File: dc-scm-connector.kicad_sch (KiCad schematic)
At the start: 2 parts, among them J1 Socket_DC-SCM-2.1_2x84_Rev-1-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

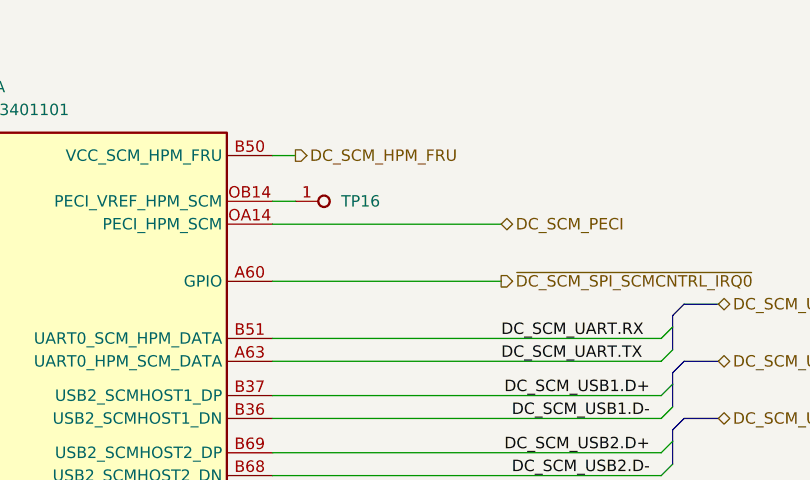
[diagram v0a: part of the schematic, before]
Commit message: [#93949] Change testpads to 1.5mm, change QSPI and UART testpad to smd technology
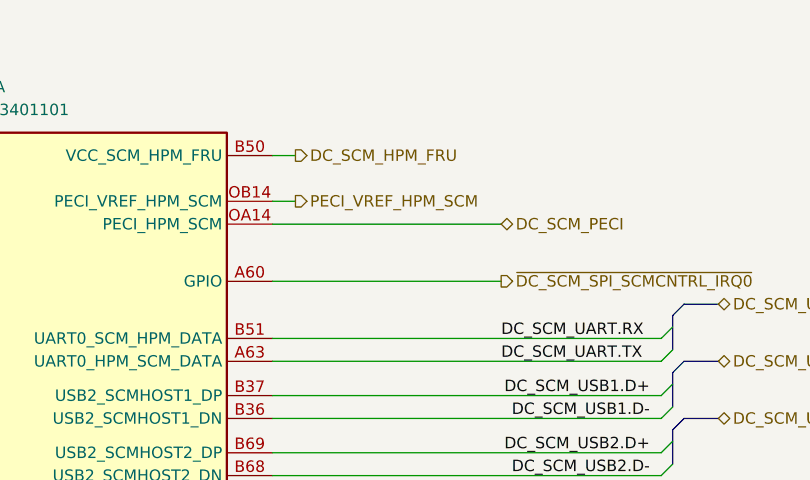
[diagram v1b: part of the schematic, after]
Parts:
- removed TP16: TP_0.75mm_SMD, antmicro-footprints:TP_SMD_0.75mm, symbol antmicroTestPoints:TP_0.75mm_SMD
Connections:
- net PECI_VREF_HPM_SCM: now reaches J1.OB14 (PECI_VREF_HPM_SCM)
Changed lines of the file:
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@@
+		)
+	)
+	(hierarchical_label "PECI_VREF_HPM_SCM"
+		(shape output)
+		(at 149.86 49.53 0)
+		(effects
+			(font
+				(size 1.27 1.27)
+			)
+			(justify left)
 		)
 	)
@@
 				)
 			)
-		)
-	)
-	(symbol
-		(lib_id "antmicroTestPoints:TP_0.75mm_SMD")
-		(at 149.86 49.53 0)
-		(unit 1)
-		(exclude_from_sim no)
-		(in_bom no)
-		(on_board yes)
-		(dnp no)
-		(property "Reference" "TP16"
-			(at 154.94 49.53 0)
-			(effects
-				(font
-					(size 1.27 1.27)
-					(thickness 0.15)
-				)
-				(justify left)
-			)
-		)
-		(property "Value" "TP_0.75mm_SMD"
-			(at 160.02 53.34 0)
-			(effects
-				(font
-					(size 1.27 1.27)
-					(thickness 0.15)
-				)
-				(justify left bottom)
-				(hide yes)
-			)
-		)
-		(property "Footprint" "antmicro-footprints:TP_SMD_0.75mm"
-			(at 160.02 55.88 0)
-			(effects
-				(font
-					(size 1.27 1.27)
-					(thickness 0.15)
-				)
-				(justify left bottom)
-				(hide yes)
-			)
-		)
-		(property "Datasheet" ""
-			(at 167.64 62.23 0)
-			(effects
-				(font
-					(size 1.27 1.27)
-					(thickness 0.15)
-				)
-				(justify left bottom)
-				(hide yes)
-			)
-		)
-		(property "Description" "SMT test point"
-			(at 160.655 63.5 0)
-			(effects
-				(font
-					(size 1.27 1.27)
-				)
-				(justify left bottom)
-				(hide yes)
-			)
-		)
-		(property "MPN" ""
-			(at 160.655 60.96 0)
-			(effects
-				(font
-					(size 1.27 1.27)
-					(thickness 0.15)
-				)
-				(justify left bottom)
-				(hide yes)
-			)
-		)
-		(property "Manufacturer" ""
-			(at 160.655 55.88 0)
-			(effects
-				(font
-					(size 1.27 1.27)
-					(thickness 0.15)
-				)
-				(justify left bottom)
-				(hide yes)
-			)
-		)
-		(property "Author" "Antmicro"
-			(at 160.02 58.42 0)
-			(effects
-				(font
-					(size 1.27 1.27)
-					(thickness 0.15)
-				)
-				(justify left bottom)
-				(hide yes)
-			)
-		)
-		(property "License" "Apache-2.0"
-			(at 160.02 60.96 0)
-			(effects
-				(font
-					(size 1.27 1.27)
-					(thickness 0.15)
-				)
-				(justify left bottom)
-				(hide yes)
-			)
-		)
-		(pin "1"
-		)
-		(instances
-			(project "bmc-breakout-board"
-				(path "/5d67ef28-5805-4f87-b722-2926dabf7f6e/bae8cef5-57a9-4ec0-acbe-6dac48c5cdf5"
-					(reference "TP16")
-					(unit 1)
-				)
-			)

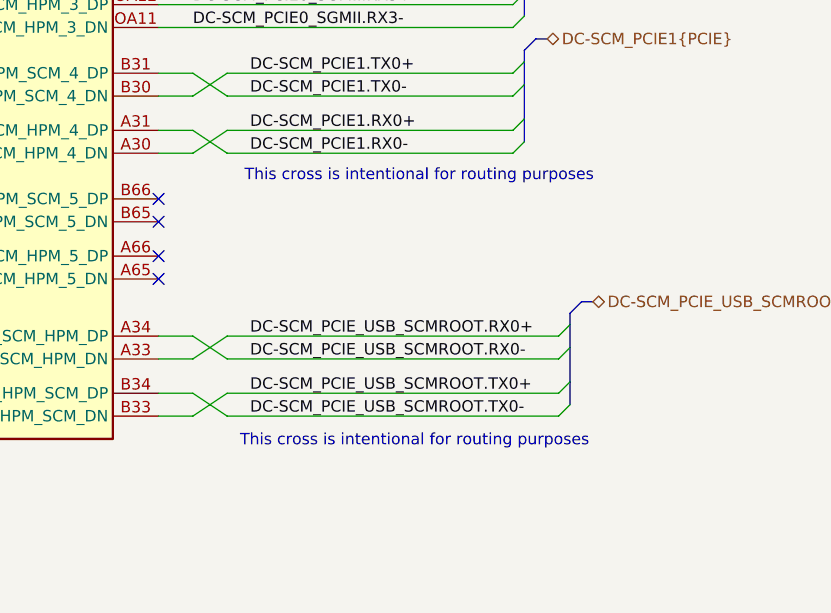
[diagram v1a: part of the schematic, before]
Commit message: [#93949] Align items to grid, change TP for UART
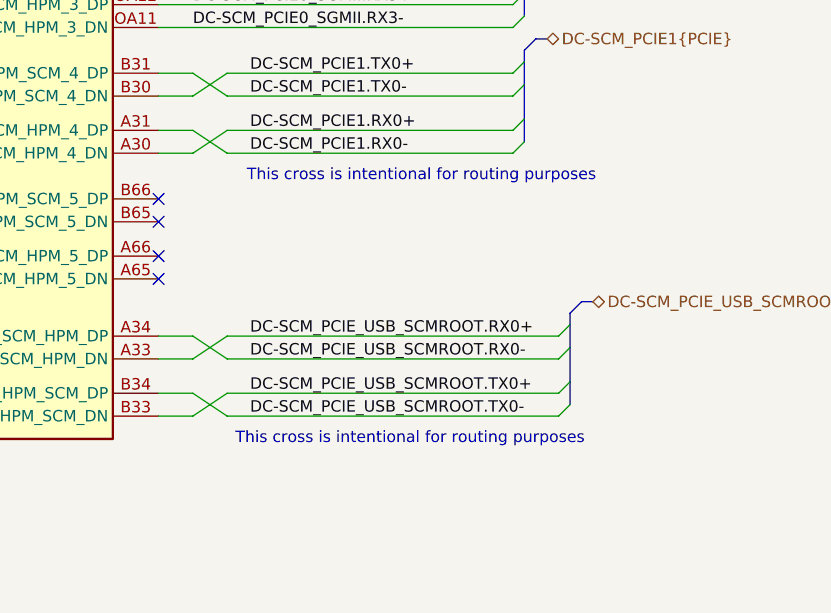
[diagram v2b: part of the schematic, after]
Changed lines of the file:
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@@
 	(text "This cross is intentional for routing purposes"
 		(exclude_from_sim no)
-		(at 340.106 167.64 0)
+		(at 340.36 167.64 0)
 		(effects
 			(font
@@
 	(text "This cross is intentional for routing purposes"
 		(exclude_from_sim no)
-		(at 339.598 197.104 0)
+		(at 339.09 196.85 0)
 		(effects
 			(font
